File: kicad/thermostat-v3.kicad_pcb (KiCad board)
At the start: 2 copper layers, 140 x 64 mm, 101 parts, among them J1 HVAC R C W Y G, J2 USB-C, J3 Stemma QT, J4 2.9in EPD FPC, Q1 AO3400A, Q2 T435-600B, Q3 T435-600B, Q4 T435-600B, SW1 RESET, SW2 BOOT, SW3 UP, SW4 DOWN, SW5 MODE, U1 LMR16006XDDCR, U2 USBLC6-2SC6, U3 ESP32-C6-WROOM-1-N8, U4 STWD100NYWY3F, U5 SHT40-AD1B, U6 MOC3063S, U7 MOC3063S, U8 MOC3063S

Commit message: Rev 11: Q2-Q4 T435-600B -> T405-600B-TR (C283473, IH 10 mA); refresh bom_prices; regen fab
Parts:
- Q2, Q3, Q4: value T435-600B -> T405-600B
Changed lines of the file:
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@@
 			)
 		)
-		(property "Value" "T435-600B"
+		(property "Value" "T405-600B"
 			(at 0 6.29 0)
 			(layer "F.Fab")
@@
 			)
 		)
-		(property "LCSC Part" "C18186224"
+		(property "LCSC Part" "C283473"
 			(at 0 0 0)
 			(layer "F.Fab")
@@
 			)
 		)
-		(property "LCSC" "C145128"
+		(property "LCSC" "C283473"
 			(at 0 0 0)
 			(layer "F.SilkS")
@@
 			)
 		)
-		(property "Value" "T435-600B"
+		(property "Value" "T405-600B"
 			(at 0 6.29 0)
 			(layer "F.Fab")
@@
 			)
 		)
-		(property "LCSC Part" "C18186224"
+		(property "LCSC Part" "C283473"
 			(at 0 0 0)
 			(layer "F.Fab")
@@
 			)
 		)
-		(property "LCSC" "C145128"
+		(property "LCSC" "C283473"
 			(at 0 0 0)
 			(layer "F.SilkS")
@@
 			)
 		)
-		(property "Value" "T435-600B"
+		(property "Value" "T405-600B"
 			(at 0 6.29 0)
 			(layer "F.Fab")
@@
 			)
 		)
-		(property "LCSC Part" "C18186224"
+		(property "LCSC Part" "C283473"
 			(at 0 0 0)
 			(layer "F.Fab")
@@
 			)
 		)
-		(property "LCSC" "C145128"
+		(property "LCSC" "C283473"
 			(at 0 0 0)
 			(layer "F.SilkS")

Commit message: Rev 12: D2 SMBJ40A -> SMBJ40CA (JLC preferred-extended, no loading fee); refresh prices
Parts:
- D2: value SMBJ40A -> SMBJ40CA
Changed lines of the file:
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@@
 			)
 		)
-		(property "Value" "SMBJ40A"
+		(property "Value" "SMBJ40CA"
 			(at 0 4 180)
 			(layer "F.Fab")
@@
 			)
 		)
-		(property "LCSC Part" "C114003"
+		(property "LCSC Part" "C19077590"
 			(at 0 0 180)
 			(layer "F.Fab")
@@
 			)
 		)
-		(property "LCSC" "C114003"
+		(property "LCSC" "C19077590"
 			(at 0 0 180)
 			(layer "F.SilkS")

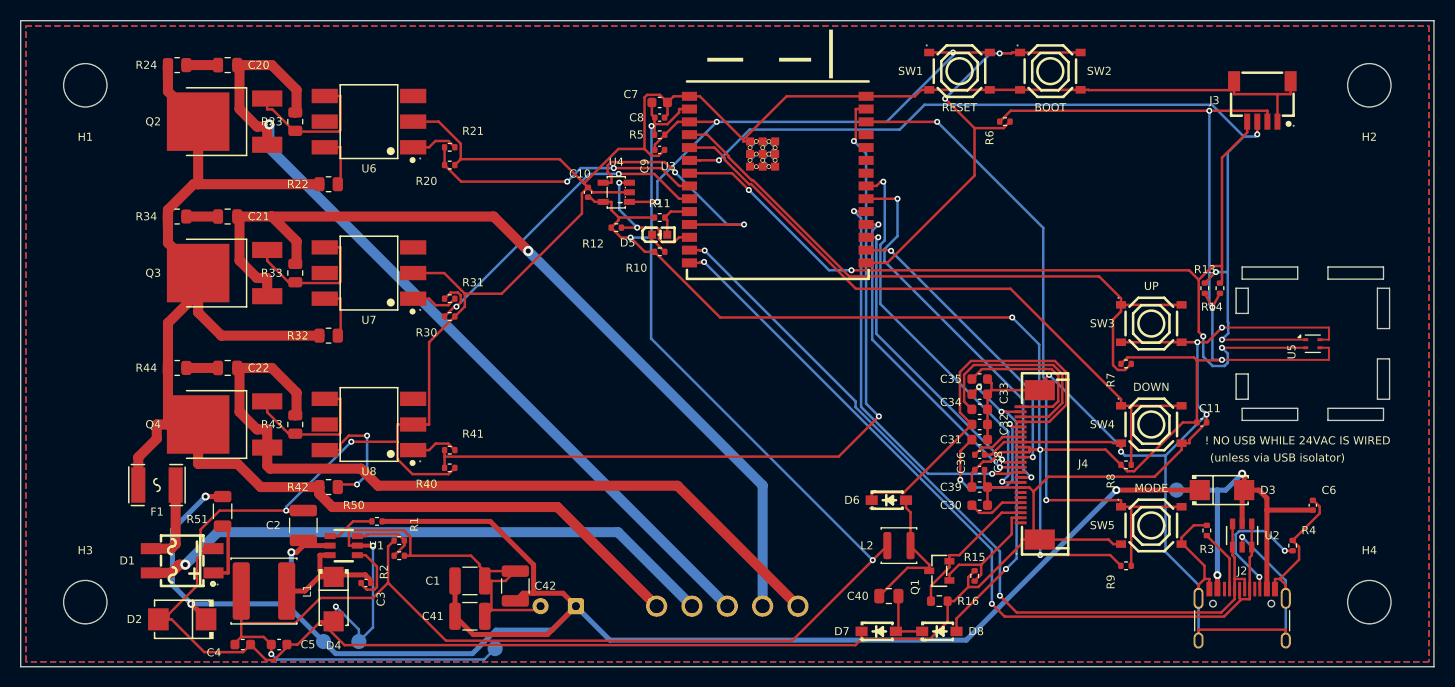
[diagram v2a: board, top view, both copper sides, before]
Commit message: Rev 13: Ferdinand review fixes - opto-gap + 0.6mm HV/LV clearance rules and reroutes, neutral footprint names, MB10S symbol pins, USB silk note, part-plan rewrite
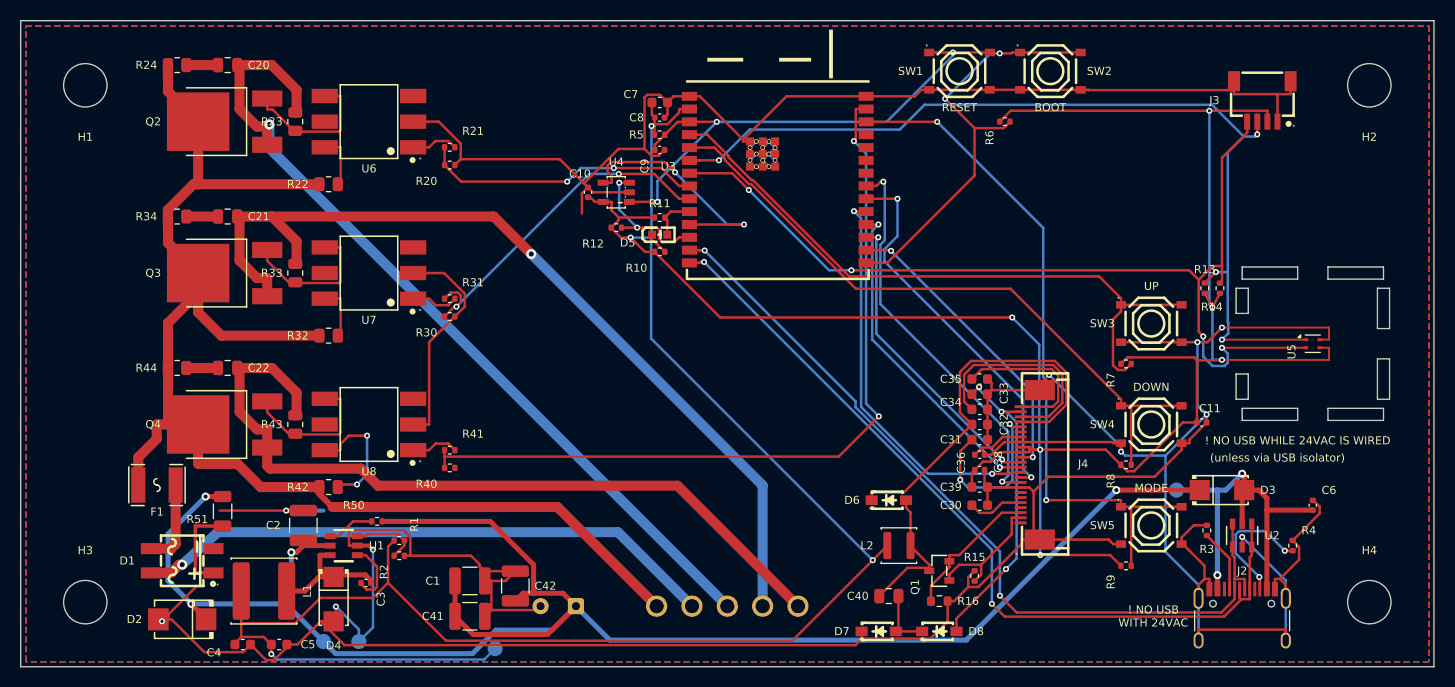
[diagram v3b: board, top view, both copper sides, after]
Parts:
- C43: footprint Capacitor_THT:CP_Radial_D8.0mm_P3.50mm -> tstat:CP_Radial_D8.0mm_P3.50mm
- D2: footprint tstat:SMB_SMBJ40A -> tstat:D_SMB_TVS
- J2: footprint Connector_USB:USB_C_Receptacle_HRO_TYPE-C-31-M-12 -> tstat:USB_C_Receptacle_HRO_TYPE-C-31-M-12
- Q2, Q3, Q4: footprint tstat:TO-252_BT136S -> tstat:TO-252-2_TRIAC_DPAK
- TP1, TP2, TP3, TP4: footprint TestPoint:TestPoint_Pad_D1.5mm -> tstat:TestPoint_Pad_D1.5mm
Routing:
- net GND: track 565.8 -> 518.8 mm
- net VIN_RECT: track 6.64 -> 9.15 mm
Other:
- board text added: "! NO USB WITH 24VAC"

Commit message: rev 14: opto gaps F+B keepouts (0 mm² copper), HV clearances to 0.8 mm, 1.0 mm USB warnings, fresh gerbers
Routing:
- net HVAC_W: track 85.8 -> 96.0 mm
- net OPTO_MT2_G: track 12.4 -> 7.61 mm
- net VIN_RECT: track 9.15 -> 9.68 mm
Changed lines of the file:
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@@
 		)
 	)
-	(gr_text "! NO USB WHILE 24VAC IS WIRED"
-		(at 226.5 141.6 0)
+	(gr_text "! NO USB WHILE\n24VAC IS WIRED"
+		(at 226.5 141.8 0)
 		(layer "F.SilkS")
 		(effects
 			(font
-				(size 0.8 0.8)
-				(thickness 0.12)
+				(size 1 1)
+				(thickness 0.15)
 			)
 		)
@@
 	)
 	(gr_text "(unless via USB isolator)"
-		(at 224.5 143.3 0)
+		(at 228 144.2 0)
 		(layer "F.SilkS")
 		(effects
@@
 	)
 	(gr_text "! NO USB\nWITH 24VAC"
-		(at 212.2 159 0)
+		(at 211 159 0)
 		(layer "F.SilkS")
 		(effects
 			(font
-				(size 0.8 0.8)
+				(size 1 1)
 				(thickness 0.15)
 			)
@@
 	)
 	(segment
-		(start 130.878999 148.179)
-		(end 153.179 148.179)
+		(start 130.679 147.979)
+		(end 152.979 147.979)
 		(width 1)
 		(layer "F.Cu")
@@
 	(segment
 		(start 129.588 146.888)
-		(end 130.878999 148.179)
+		(end 130.679 147.979)
 		(width 0.6)
 		(layer "F.Cu")
@@
 	)
 	(segment
-		(start 153.179 148.179)
+		(start 152.979 147.979)
 		(end 163 158)
 		(width 1)
@@
 	)
 	(segment
-		(start 170 158)
+		(start 124.629 130)
 		(end 124.629 112.629)
 		(width 1)
@@
 	)
 	(segment
+		(start 170 158)
+		(end 142 130)
+		(width 1)
+		(layer "B.Cu")
+		(net 3)
+	)
+	(segment
+		(start 142 130)
+		(end 124.629 130)
+		(width 1)
+		(layer "B.Cu")
+		(net 3)
+	)
+	(segment
 		(start 124.629 112.629)
 		(end 124.629 110.281)
@@
 	)
 	(segment
+		(start 117.3 153.45)
+		(end 116.925 153.075)
+		(width 0.35)
+		(layer "F.Cu")
+		(net 7)
+	)
+	(segment
 		(start 120 150.062)
 		(end 120 150.0625)
@@
 	)
 	(segment
-		(start 117.3 150.06)
+		(start 116.925 150.06)
 		(end 120 150.06)
 		(width 0.35)
@@
 	(segment
 		(start 117.3 154.7)
-		(end 117.3 150.06)
+		(end 117.3 153.45)
+		(width 0.35)
+		(layer "F.Cu")
+		(net 7)
+	)
+	(segment
+		(start 116.925 153.075)
+		(end 116.925 150.06)
 		(width 0.35)
 		(layer "F.Cu")
@@
 	(segment
 		(start 118.316 147.138)
-		(end 114.6 150.854)
+		(end 114.45 151.004)
 		(width 0.5)
 		(layer "B.Cu")
@@
 	)
 	(segment
-		(start 114.6 155.467)
+		(start 114.45 155.318)
 		(end 116.902 157.77)
 		(width 0.5)
@@
 	)
 	(segment
-		(start 114.6 150.854)
-		(end 114.6 155.467)
+		(start 114.45 151.004)
+		(end 114.45 155.318)
 		(width 0.5)
 		(layer "B.Cu")
@@
 	)
 	(segment
-		(start 132.51 141.109)
-		(end 134.313 141.109)
-		(width 0.25)
-		(layer "F.Cu")
-		(net 50)
-	)
-	(segment
-		(start 131.697 141.923)
-		(end 132.51 141.109)
-		(width 0.25)
-		(layer "F.Cu")
-		(net 50)
-	)
-	(segment
-		(start 131.697 142.54)
-		(end 131.697 141.923)
-		(width 0.25)
-		(layer "F.Cu")
-		(net 50)
-	)
-	(segment
 		(start 131.4125 146.1995)
 		(end 131.412 146.2)
@@
 		(net 50)
 	)
+	(segment
+		(start 131.697 142.54)
+		(end 131.9 143.05)
+		(width 0.25)
+		(layer "F.Cu")
+		(net 50)
+	)
 	(via
-		(at 134.313 141.109)
+		(at 133.316 145.94)
 		(size 0.6)
 		(drill 0.3)
@@
 	)
 	(via
-		(at 133.316 145.94)
+		(at 131.9 143.05)
 		(size 0.6)
 		(drill 0.3)
@@
 	)
 	(segment
-		(start 134.313 144.944)
-		(end 134.313 141.109)
+		(start 131.9 143.05)
+		(end 131.9 144.524)
 		(width 0.25)
 		(layer "B.Cu")
@@
 	)
 	(segment
-		(start 133.316 145.94)
-		(end 134.313 144.944)
+		(start 131.9 144.524)
+		(end 133.316 145.94)
 		(width 0.25)
 		(layer "B.Cu")
@@
 	)
 	(zone
-		(net 0)
-		(net_name "")
+		(net 8)
+		(net_name "GND")
 		(layer "F.Cu")
-		(name "OPTO_GAP_U7")
 		(hatch edge 0.5)
-		(connect_pads
-			(clearance 0)
+		(connect_pads yes
+			(clearance 0.3)
 		)
 		(min_thickness 0.25)
 		(filled_areas_thickness no)
-		(keepout
-			(tracks allowed)
-			(vias allowed)
-			(pads allowed)
-			(copperpour allowed)
-			(footprints allowed)
-		)
-		(placement
-			(enabled no)
-			(sheetname "")
-		)
-		(fill
+		(fill yes
 			(thermal_gap 0.5)
 			(thermal_bridge_width 0.5)
@@
 		(polygon
 			(pts
-				(xy 131.6 121.4) (xy 137.4 121.4) (xy 137.4 128.6) (xy 131.6 128.6)
+				(xy 100.5 100.5) (xy 239.5 100.5) (xy 239.5 163.5) (xy 100.5 163.5)
 			)
 		)
@@
 		(net 0)
 		(net_name "")
-		(layer "F.Cu")
-		(name "OPTO_GAP_U6")
+		(layers "F.Cu" "B.Cu")
 		(hatch edge 0.5)
 		(connect_pads
@@
 		(filled_areas_thickness no)
 		(keepout
-			(tracks allowed)
-			(vias allowed)
+			(tracks not_allowed)
+			(vias not_allowed)
 			(pads allowed)
-			(copperpour allowed)
+			(copperpour not_allowed)
 			(footprints allowed)
 		)
@@
 		(polygon
 			(pts
-				(xy 131.6 106.4) (xy 137.4 106.4) (xy 137.4 113.6) (xy 131.6 113.6)
+				(xy 219.9 134.5) (xy 222.1 134.5) (xy 222.1 138) (xy 219.9 138)
 			)
 		)
 	)
 	(zone
-		(net 8)
-		(net_name "GND")
-		(layer "F.Cu")
+		(net 0)
+		(net_name "")
+		(layers "F.Cu" "B.Cu")
 		(hatch edge 0.5)
-		(connect_pads yes
-			(clearance 0.3)
+		(connect_pads
+			(clearance 0)
 		)
 		(min_thickness 0.25)
 		(filled_areas_thickness no)
-		(fill yes
+		(keepout
+			(tracks not_allowed)
+			(vias not_allowed)
+			(pads allowed)
+			(copperpour not_allowed)
+			(footprints allowed)
+		)
+		(placement
+			(enabled no)
+			(sheetname "")
+		)
+		(fill
 			(thermal_gap 0.5)
 			(thermal_bridge_width 0.5)
@@
 		(polygon
 			(pts
-				(xy 100.5 100.5) (xy 239.5 100.5) (xy 239.5 163.5) (xy 100.5 163.5)
+				(xy 233.9 133) (xy 236.1 133) (xy 236.1 138) (xy 233.9 138)
 			)
 		)
@@
 		(net 0)
 		(net_name "")
-		(layer "F.Cu")
-		(name "OPTO_GAP_U8")
+		(layers "F.Cu" "B.Cu")
 		(hatch edge 0.5)
 		(connect_pads
@@
 		(filled_areas_thickness no)
 		(keepout
-			(tracks allowed)
-			(vias allowed)
+			(tracks not_allowed)
+			(vias not_allowed)
 			(pads allowed)
-			(copperpour allowed)
+			(copperpour not_allowed)
 			(footprints allowed)
 		)
@@
 		(polygon
 			(pts
-				(xy 131.6 136.4) (xy 137.4 136.4) (xy 137.4 143.6) (xy 131.6 143.6)
+				(xy 220.5 137.9) (xy 227 137.9) (xy 227 140.1) (xy 220.5 140.1)
 			)
 		)
@@
 		(polygon
 			(pts
-				(xy 219.9 134.5) (xy 222.1 134.5) (xy 222.1 138) (xy 219.9 138)
+				(xy 229 137.9) (xy 235.5 137.9) (xy 235.5 140.1) (xy 229 140.1)
 			)
 		)
@@
 		(net_name "")
 		(layers "F.Cu" "B.Cu")
+		(name "OPTO_GAP_U7")
 		(hatch edge 0.5)
 		(connect_pads
@@
 		(polygon
 			(pts
-				(xy 233.9 133) (xy 236.1 133) (xy 236.1 138) (xy 233.9 138)
+				(xy 132.3 121.4) (xy 137.1 121.4) (xy 137.1 128.6) (xy 132.3 128.6)
 			)
 		)
@@
 		(polygon
 			(pts
-				(xy 220.5 137.9) (xy 227 137.9) (xy 227 140.1) (xy 220.5 140.1)
+				(xy 229 123.9) (xy 235.5 123.9) (xy 235.5 126.1) (xy 229 126.1)
 			)
 		)
@@
 		(net_name "")
 		(layers "F.Cu" "B.Cu")
+		(name "ANT_KEEPOUT")
 		(hatch edge 0.5)
 		(connect_pads
@@
 		(polygon
 			(pts
-				(xy 229 137.9) (xy 235.5 137.9) (xy 235.5 140.1) (xy 229 140.1)
+				(xy 161 100) (xy 189 100) (xy 189 106.4) (xy 161 106.4)
 			)
 		)
@@
 		(net_name "")
 		(layers "F.Cu" "B.Cu")
+		(name "OPTO_GAP_U6")
 		(hatch edge 0.5)
 		(connect_pads
@@
 		(polygon
 			(pts
-				(xy 229 123.9) (xy 235.5 123.9) (xy 235.5 126.1) (xy 229 126.1)
+				(xy 132.3 106.4) (xy 137.1 106.4) (xy 137.1 113.6) (xy 132.3 113.6)
 			)
 		)
@@
 		(net_name "")
 		(layers "F.Cu" "B.Cu")
-		(name "ANT_KEEPOUT")
 		(hatch edge 0.5)
 		(connect_pads
@@
 		(polygon
 			(pts
-				(xy 161 100) (xy 189 100) (xy 189 106.4) (xy 161 106.4)
+				(xy 233.9 126) (xy 236.1 126) (xy 236.1 131) (xy 233.9 131)
 			)
 		)
@@
 		(polygon
 			(pts
-				(xy 233.9 126) (xy 236.1 126) (xy 236.1 131) (xy 233.9 131)
+				(xy 219.9 126) (xy 222.1 126) (xy 222.1 129.5) (xy 219.9 129.5)
 			)
 		)
@@
 		(polygon
 			(pts
-				(xy 219.9 126) (xy 222.1 126) (xy 222.1 129.5) (xy 219.9 129.5)
+				(xy 220.5 123.9) (xy 227 123.9) (xy 227 126.1) (xy 220.5 126.1)
 			)
 		)
@@
 		(net_name "")
 		(layers "F.Cu" "B.Cu")
+		(name "ISLAND")
 		(hatch edge 0.5)
 		(connect_pads
@@
 		(filled_areas_thickness no)
 		(keepout
-			(tracks not_allowed)
-			(vias not_allowed)
+			(tracks allowed)
+			(vias allowed)
 			(pads allowed)
 			(copperpour not_allowed)
@@
 		(polygon
 			(pts
-				(xy 220.5 123.9) (xy 227 123.9) (xy 227 126.1) (xy 220.5 126.1)
+				(xy 220.4 124.4) (xy 235.6 124.4) (xy 235.6 139.6) (xy 220.4 139.6)
 			)
 		)
@@
 		(net_name "")
 		(layers "F.Cu" "B.Cu")
-		(name "ISLAND")
+		(name "OPTO_GAP_U8")
 		(hatch edge 0.5)
 		(connect_pads
@@
 		(filled_areas_thickness no)
 		(keepout
-			(tracks allowed)
-			(vias allowed)
+			(tracks not_allowed)
+			(vias not_allowed)
 			(pads allowed)
 			(copperpour not_allowed)
@@
 		(polygon
 			(pts
-				(xy 220.4 124.4) (xy 235.6 124.4) (xy 235.6 139.6) (xy 220.4 139.6)
+				(xy 132.3 136.4) (xy 137.1 136.4) (xy 137.1 143.6) (xy 132.3 143.6)
 			)
 		)
